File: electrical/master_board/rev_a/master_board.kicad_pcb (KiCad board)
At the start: 2 copper layers, 145.3 x 156.6 mm, 180 parts, among them CN1 USB3140-30-230-1-C;VERT,2.3FL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, CN10 WOW_OUT;M2x6S, CN2 USB3140-30-230-1-C;VERT,2.3FL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, CN5 LIDAR_ADAPTER;2xF1x3+F1x2, CN6 SERVO;F1x3, CN7 SERVO;F1x3, CN8 SERVO;F1x3, CN81 HCSR04LP;F1X4, CN82 HCSR04LP;F1X4, CN83 HCSR04LP;F1X4, CN84 HCSR04LP;F1X4, CN85 HCSR04LP;F1X4, CN86 HCSR04LP;F1X4, CN87 HCSR04LP;F1X4, CN88 MIKROBUS_MATE;SMALL, CN89 MIKROBUS_MATE;MEDIUM, CN9 SERVO;F1x3, CN90 STADAPTER;F2x4, CN91 HR2_ENCODER;2xF1x3, CN92 HR2_ENCODER;2xF1x3, CN93 POLOLU_U3V70F9;F1x4+F1x5, CN94 RASPI;F2X20, CN95 NUCLEO-F767ZI;2xF2x35, Q1 2N2222;SOT23, Q10 2N7000;SOT23, Q11 2N7000;SOT23, Q12 2N7000;SOT23, Q13 2N7000;SOT23, Q14 2N7000;SOT23, Q15 2N7000;SOT23, Q16 2N7000;SOT23, Q17 2N7000;SOT23, Q18 2N7000;SOT23, Q19 2N7000;SOT23, Q2 POWER_PFET_GSD, Q20 2N7000;SOT23, Q21 PFET_6A_GSD;SOT23, Q22 2N7000;SOT23, Q3 2N2222;SOT23, Q4 2N7000;SOT23, Q5 2N7000;SOT23, Q6 2N7000;SOT23, Q7 2N7000;SOT23, Q8 2N7000;SOT23, Q9 2N7000;SOT23, SW1 BUTTON;6x3.5, SW2 BUTTON;6x3.5, SW3 BUTTON;6x3.5, U1 LM66100;SOT363, U10 CD450B;TTSOP16, U11 SN74HCS595;TTSOP16, U12 SN74HCS595;TTSOP16, U13 74LVC1G11;SOT363, U14 MCP2542;SOIC8, U15 MCP2542;SOIC8, U16 74LVC1G74;TSSOP8, U17 CPC1017N;SOP4W3.8L4.1, U18 CPC1017N;SOP4W3.8L4.1, U2 MCP7940;SOIC8, U3 CAT24C32;SOIC8, U4 DRV8833PWPR;16HTSSOP, U5 SN74HCS595;TTSOP16, U6 SN74HCS166;TTSOP16, U7 SN74HCS166;TTSOP16, U8 SN74HCS595;TTSOP16, U9 CD450B;TTSOP16, X1 32.768kHz9pF;3.2x1.5

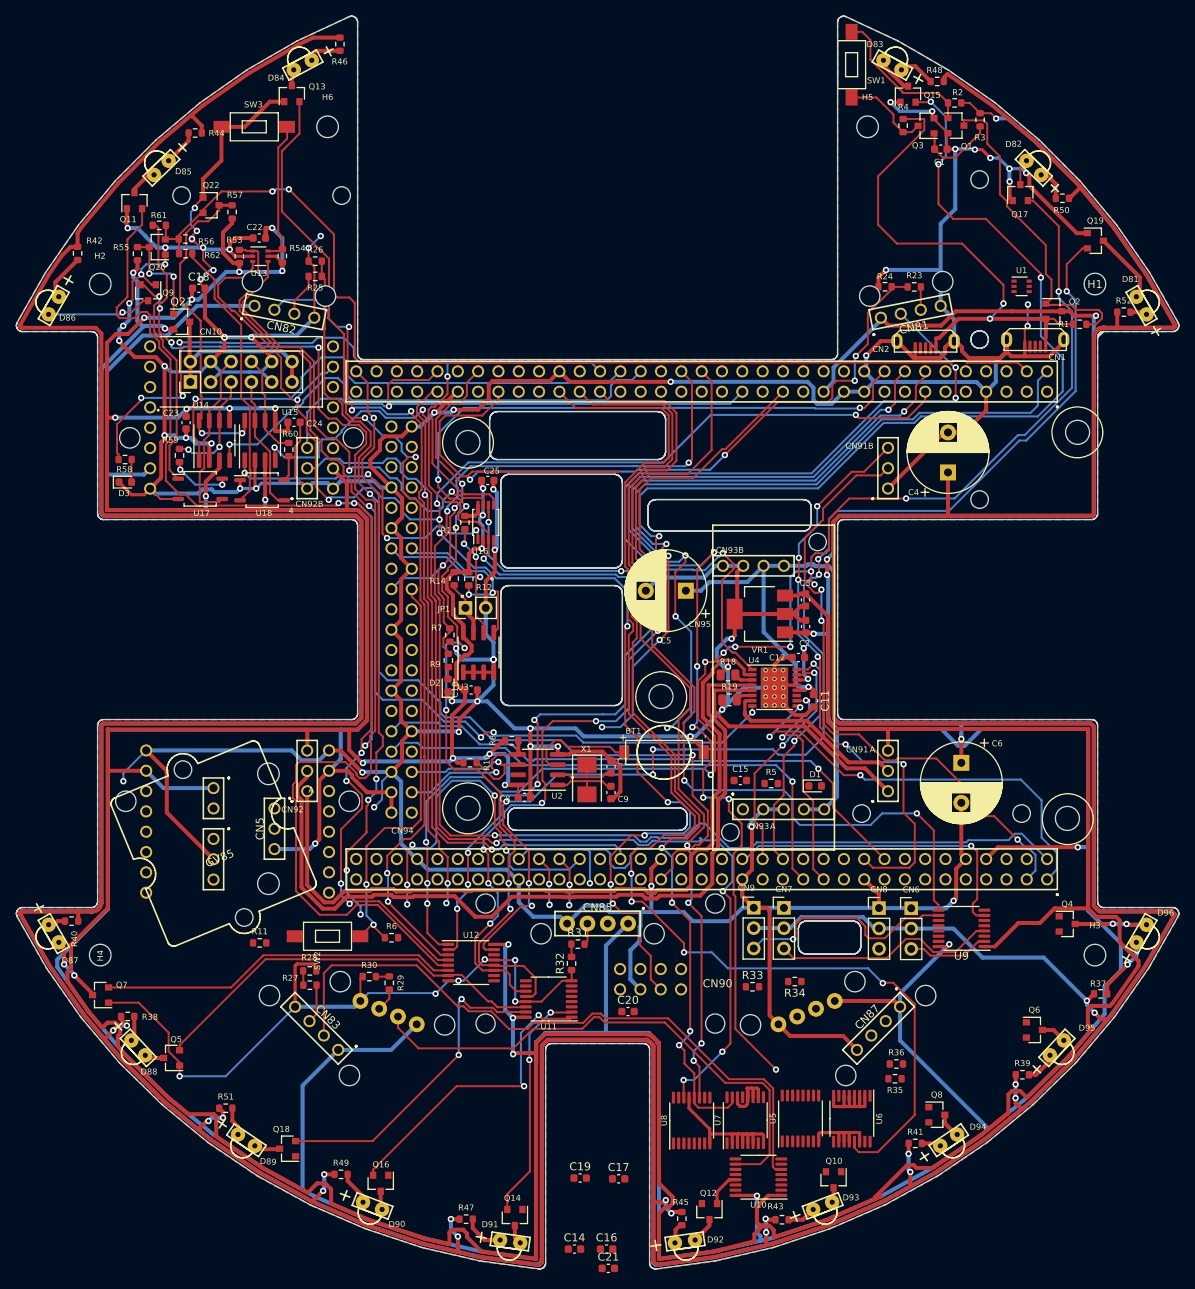
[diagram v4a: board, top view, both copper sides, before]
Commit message: The rats nest is getting stomped into nothingness.
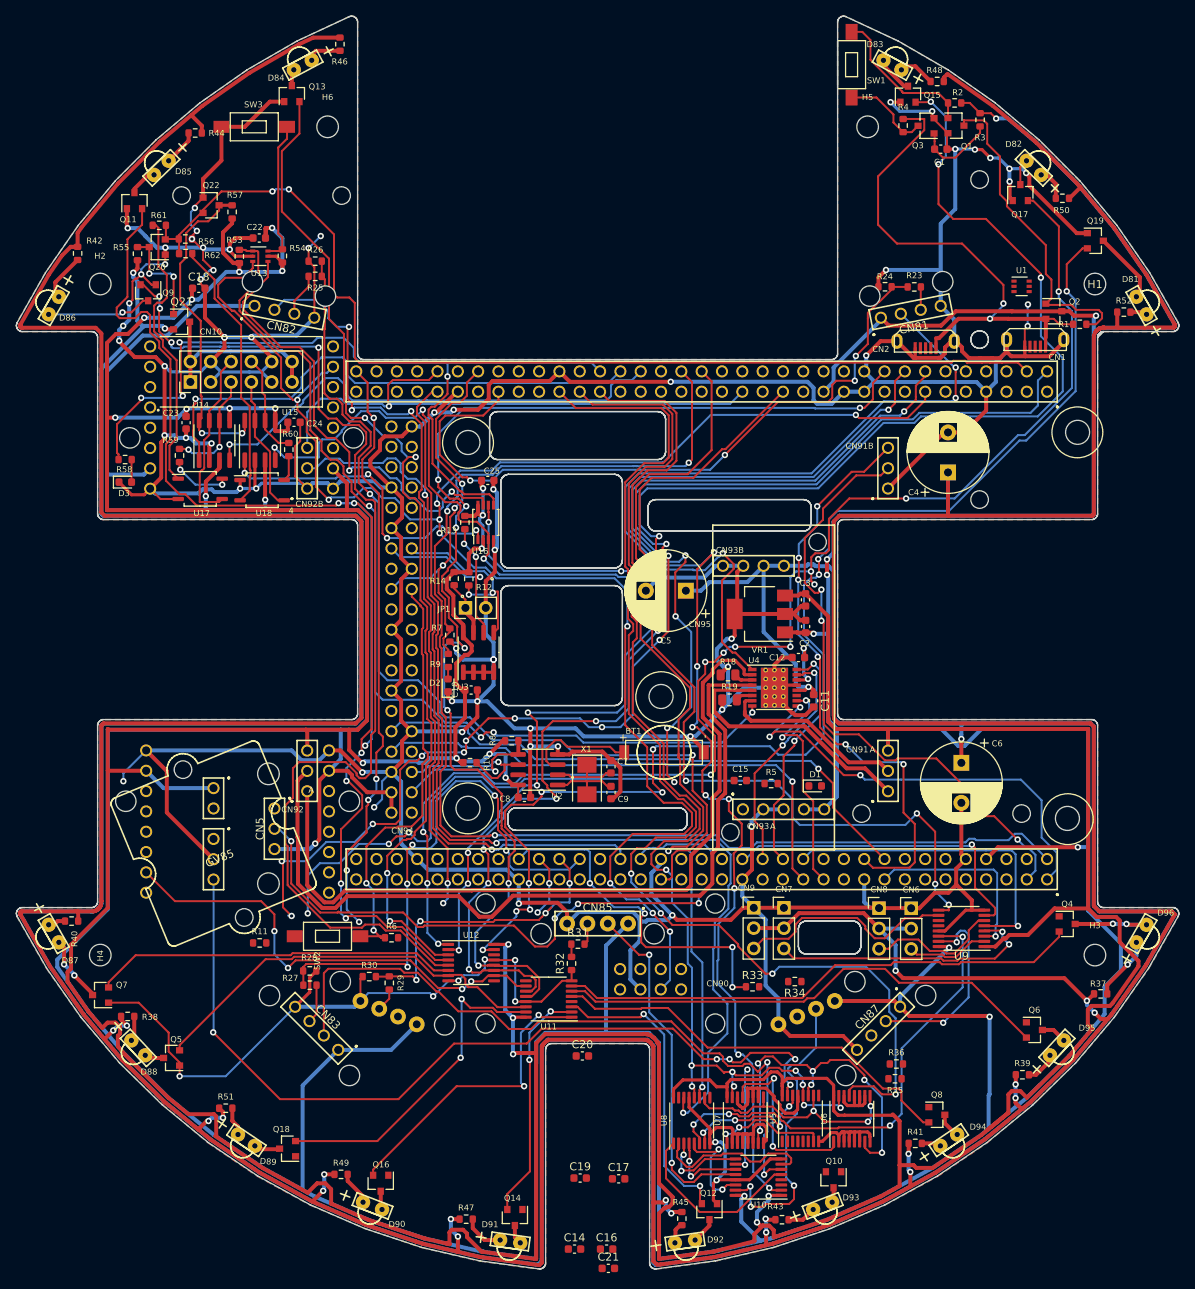
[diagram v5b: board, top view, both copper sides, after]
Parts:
- moved C20 7.96 mm to (98.1, 154.6)
- turned U6 to 90 degrees
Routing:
- net /Connectors/LDR_SPIN: track 0.00 -> 107.4 mm, vias 0 -> 5
- net /~NRST: track 226.9 -> 316.4 mm, vias 11 -> 17
- net /LDR_PWM: track 0.00 -> 83.8 mm, vias 0 -> 4
- net /LED's/LED16: track 0.00 -> 65.6 mm
- net /SWCLK: track 83.3 -> 148.4 mm, vias 4 -> 8
- net /LED's/LED15: track 0.00 -> 62.6 mm
- net /SWDIO: track 81.1 -> 141.1 mm, vias 4 -> 11
- net /Sonars and Servos/TRIG7: track 0.00 -> 59.4 mm, vias 0 -> 4
- net /Sonars and Servos/TRIG4_5V: track 67.2 -> 13.2 mm, vias 0 -> 2
- net /LED's/LED14: track 0.00 -> 51.9 mm
- net /DIO_SCK: track 108.0 -> 154.8 mm, vias 4 -> 8
- net /3.3V: track 694.8 -> 739.3 mm, vias 19 -> 21
- net /Sonars and Servos/TRIG5_5V: track 0.00 -> 43.8 mm, vias 0 -> 2
- net /SERVO3: track 0.00 -> 40.5 mm, vias 0 -> 1
- net /Sonars and Servos/TRIG6_5V: track 0.00 -> 37.6 mm, vias 0 -> 3
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
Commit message: More work thinning rats nest of unconnected wires.
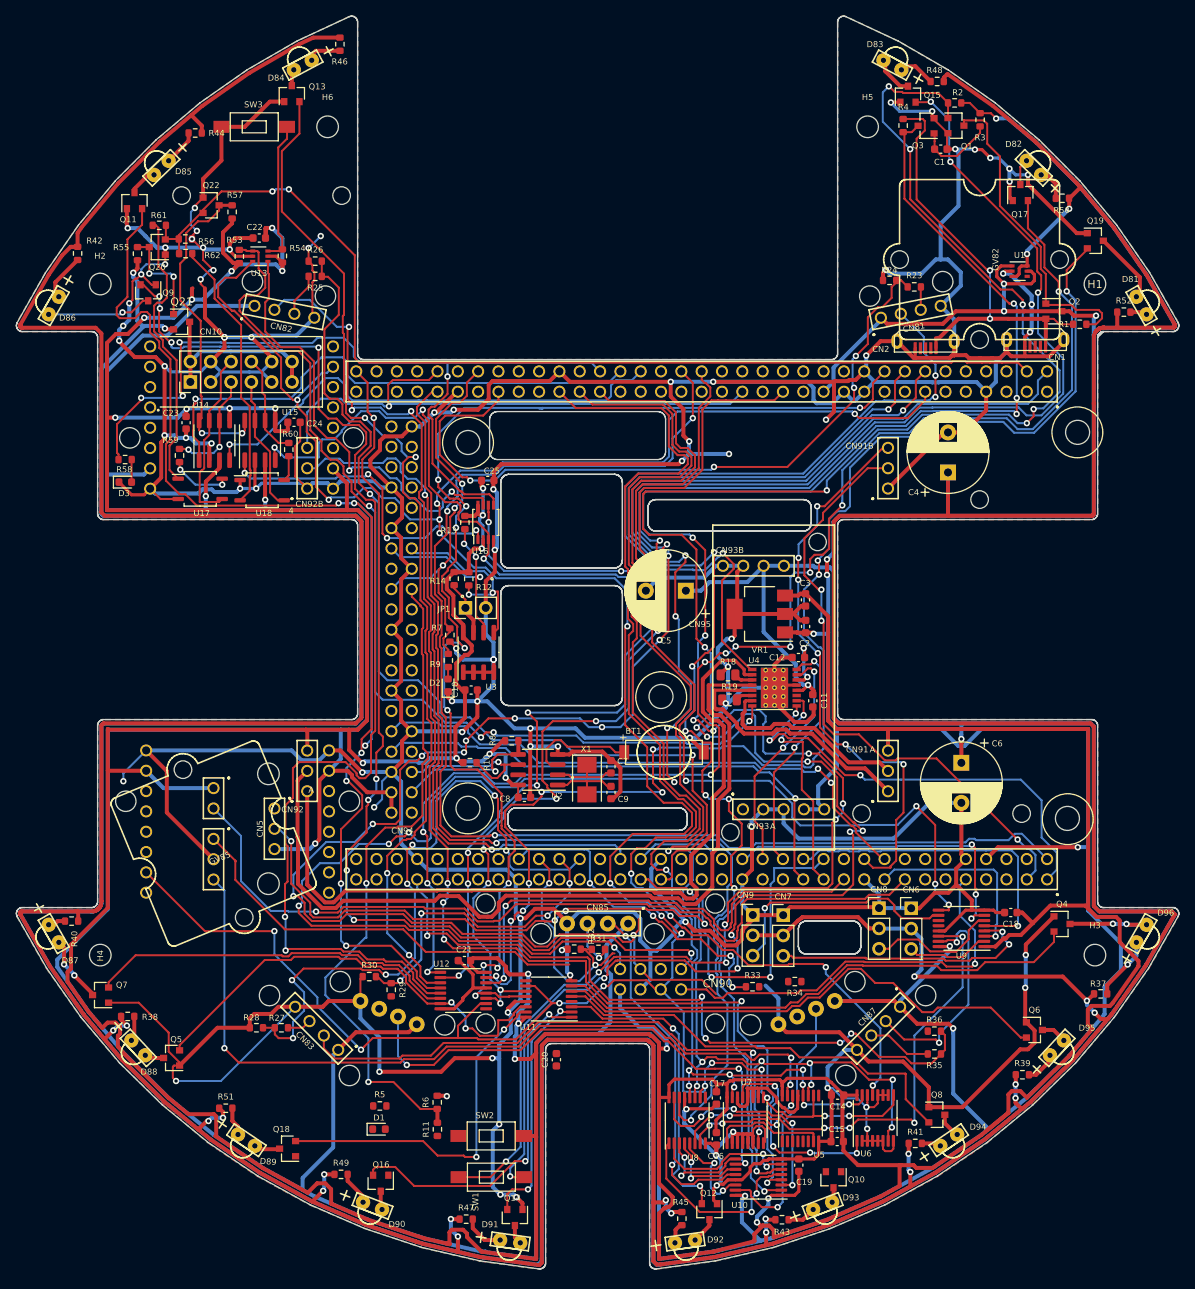
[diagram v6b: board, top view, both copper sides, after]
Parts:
- GV82: moved to F.Cu
- moved SW1 146.2 mm to (86.7, 169.7), turned to 180 degrees
- moved C18 128.0 mm to (151.7, 136.6), turned to 180 degrees
- moved D1 69.4 mm to (72.7, 163.7)
- moved R5 63.4 mm to (72.8, 160.8)
- moved C15 46.7 mm to (129.9, 165.2), turned to 180 degrees
- moved C21 42.5 mm to (83.3, 142.6), turned to 180 degrees
- moved C14 38.1 mm to (130.0, 159.4), turned to 180 degrees
- moved SW2 32.3 mm to (86.7, 164.6), turned to 0 degrees
- moved R11 32.2 mm to (80.0, 163.7), turned to 90 degrees
- moved C19 27.4 mm to (125.2, 168.2), turned to 90 degrees
- moved R6 21.4 mm to (80.0, 160.3), turned to 90 degrees
- moved C16 19.5 mm to (114.8, 164.9), turned to 270 degrees
- moved C17 15.9 mm to (114.8, 159.8), turned to 270 degrees
- moved R28 9.75 mm to (57.4, 151.0), turned to 0 degrees
- moved R27 6.41 mm to (60.5, 151.0)
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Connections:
- net Net-(C1-Pad1) renamed /Power/PWR_QBASE
- net Net-(D1-Pad2) renamed /Power/PWR_LED
- net Net-(Q1-Pad1) renamed /Power/PWR_SW_A
- net Net-(Q1-Pad3) renamed /Power/PWR_FET_G
- net Net-(Q3-Pad3) renamed /Power/PWR_SW_B
- R11 pad 1: Net-(R11-Pad1) -> /Single Board Computer/SBC_REQ
- R11 pad 2: /3.3V -> /Single Board Computer/SBC_STOP
- SW2 pad 1: /Single Board Computer/SBC_STOP -> /Single Board Computer/SBC_REQ
- SW2 pad 2: Net-(R11-Pad1) -> /3.3V
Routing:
- net /Power/PWR_SW_A: track 19.1 -> 272.1 mm, vias 0 -> 16
- net /GND: track 1107.3 -> 1356.6 mm, vias 69 -> 86
- net /Power/PWR_SW_B: track 11.0 -> 246.0 mm, vias 0 -> 14
- net /LDR_TX: track 0.00 -> 104.5 mm, vias 0 -> 1
- net /ECHO1: track 0.00 -> 88.0 mm, vias 0 -> 5
- net /Sonars and Servos/TRIG2_5V: track 95.2 -> 169.6 mm, vias 5 -> 8
- net /~NRST: track 316.4 -> 377.5 mm, vias 17 -> 20
- net /SWDIO: track 141.1 -> 202.2 mm
- net /LEDS_MOSI: track 0.00 -> 60.2 mm, vias 0 -> 2
- net /LDR_RX: track 0.00 -> 52.5 mm
- net /Sonars and Servos/TRIG4_5V: track 13.2 -> 65.3 mm, vias 2 -> 3
- net /STL_RX: track 0.00 -> 51.1 mm, vias 0 -> 1
- net /STL_TX: track 73.9 -> 121.1 mm, vias 5 -> 6
- net /A5_SCL: track 0.00 -> 46.5 mm, vias 0 -> 3
- net /SWCLK: track 148.4 -> 194.7 mm, vias 8 -> 9
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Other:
- outline, holes or cut-outs redrawn

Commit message: No unconnected traces.  Outer PCB polygon has 1 extra segment.
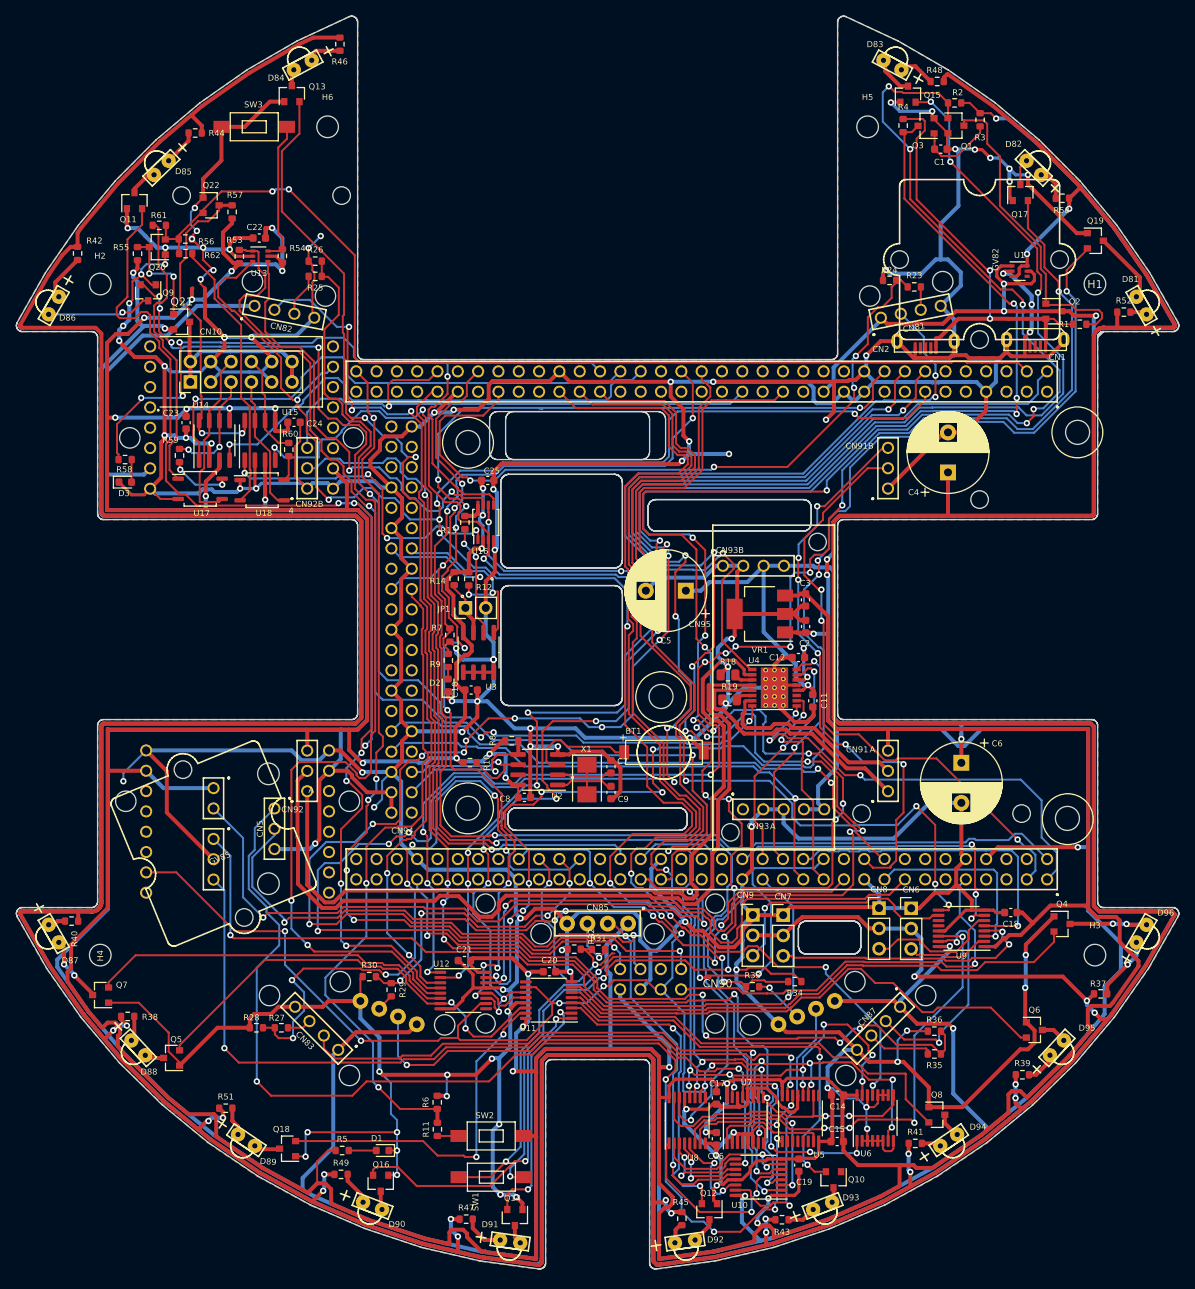
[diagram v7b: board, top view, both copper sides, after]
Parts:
- moved C20 11.0 mm to (94.0, 144.0), turned to 0 degrees
- moved R5 7.29 mm to (68.1, 166.4)
- moved D1 2.71 mm to (73.1, 166.4), turned to 180 degrees
- moved U11 0.14 mm to (93.9, 147.6)
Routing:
- net /Connectors/LDR_EN: track 0.00 -> 138.8 mm, vias 0 -> 5
- net /LDR_RX: track 52.5 -> 104.3 mm, vias 0 -> 2
- net /LED's/LED13: track 0.00 -> 51.6 mm, vias 0 -> 2
- net /GND: track 1356.6 -> 1404.5 mm, vias 86 -> 95
- net /SWDIO: track 202.2 -> 187.8 mm
- net /3.3V: track 775.3 -> 785.7 mm, vias 22 -> 24
- net /~DIO_NSS: track 149.1 -> 159.1 mm, vias 9 -> 10
- net /Sonars and Servos/ECHO6_5V: track 0.00 -> 6.39 mm, vias 0 -> 1
- net /LDR_PWM: track 85.3 -> 90.1 mm
- net /ECHO6: track 41.1 -> 45.7 mm
- net /A5_SCL: track 46.5 -> 51.0 mm
- net /9V: track 525.0 -> 521.3 mm
- net /P5V: track 770.6 -> 766.9 mm
- net /Power/PWR_LED: track 0.00 -> 3.44 mm
- net /LED's/LED6: track 145.3 -> 142.2 mm
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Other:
- outline, holes or cut-outs redrawn

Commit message: Fixed board cuts contours.
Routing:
- net /GND: track 1404.5 -> 1408.5 mm
- removed copper zone on F.Cu, net /GND
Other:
- outline, holes or cut-outs redrawn
